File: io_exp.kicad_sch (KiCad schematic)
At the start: 14 parts, among them J26 Conn_01x03, J27 Conn_01x03, J28 Conn_01x03, J4 Conn_01x03, U11 PCF8574ATS

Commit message: [WiP] add expander
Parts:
- R40, R41, R42, R43, R44, R45, R46, R47: footprint (none) -> Resistor_SMD:R_0603_1608Metric

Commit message: Add BOM
Add LCSC reference and correct few footprint acording bom
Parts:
- C34: LCSC# (none) -> ?
- J26, J27, J28, J4: LCSC# (none) -> C144394
- U11: LCSC# (none) -> C2803277
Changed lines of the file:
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@@
+			)
+		)
+		(property "LCSC#" ""
+			(at 127 63.5 0)
+			(effects
+				(font
+					(size 1.27 1.27)
+				)
+				(hide yes)
 			)
 		)
@@
 		)
 		(property "Description" "Resistor, small symbol"
+			(at 128.27 105.41 0)
+			(effects
+				(font
+					(size 1.27 1.27)
+				)
+				(hide yes)
+			)
+		)
+		(property "LCSC#" ""
 			(at 128.27 105.41 0)
 			(effects
@@
 			)
 		)
+		(property "LCSC#" "C144394"
+			(at 142.24 80.01 0)
+			(effects
+				(font
+					(size 1.27 1.27)
+				)
+				(hide yes)
+			)
+		)
 		(pin "3"
 		)
@@
 		)
 		(property "Description" "Resistor, small symbol"
+			(at 133.35 63.5 0)
+			(effects
+				(font
+					(size 1.27 1.27)
+				)
+				(hide yes)
+			)
+		)
+		(property "LCSC#" ""
 			(at 133.35 63.5 0)
 			(effects
@@
 			)
 		)
+		(property "LCSC#" "?"
+			(at 74.93 55.88 0)
+			(effects
+				(font
+					(size 1.27 1.27)
+				)
+				(hide yes)
+			)
+		)
 		(pin "1"
 		)
@@
 			)
 		)
+		(property "LCSC#" ""
+			(at 134.62 91.44 0)
+			(effects
+				(font
+					(size 1.27 1.27)
+				)
+				(hide yes)
+			)
+		)
 		(pin "2"
 		)
@@
 		)
 		(property "Description" "Resistor, small symbol"
+			(at 134.62 105.41 0)
+			(effects
+				(font
+					(size 1.27 1.27)
+				)
+				(hide yes)
+			)
+		)
+		(property "LCSC#" ""
 			(at 134.62 105.41 0)
 			(effects
@@
 			)
 		)
+		(property "LCSC#" "C144394"
+			(at 142.24 66.04 0)
+			(effects
+				(font
+					(size 1.27 1.27)
+				)
+				(hide yes)
+			)
+		)
 		(pin "3"
 		)
@@
 			)
 		)
+		(property "LCSC#" "C2803277"
+			(at 92.71 78.74 0)
+			(effects
+				(font
+					(size 1.27 1.27)
+				)
+				(hide yes)
+			)
+		)
 		(pin "1"
 		)
@@
 			)
 		)
+		(property "LCSC#" ""
+			(at 128.27 91.44 0)
+			(effects
+				(font
+					(size 1.27 1.27)
+				)
+				(hide yes)
+			)
+		)
 		(pin "2"
 		)
@@
 			)
 		)
+		(property "LCSC#" ""
+			(at 133.35 77.47 0)
+			(effects
+				(font
+					(size 1.27 1.27)
+				)
+				(hide yes)
+			)
+		)
 		(pin "2"
 		)
@@
 		)
 		(property "Description" "Resistor, small symbol"
+			(at 127 77.47 0)
+			(effects
+				(font
+					(size 1.27 1.27)
+				)
+				(hide yes)
+			)
+		)
+		(property "LCSC#" ""
 			(at 127 77.47 0)
 			(effects
@@
 			)
 		)
+		(property "LCSC#" "C144394"
+			(at 143.51 93.98 0)
+			(effects
+				(font
+					(size 1.27 1.27)
+				)
+				(hide yes)
+			)
+		)
 		(pin "3"
 		)
@@
 			(at 143.51 107.95 0)
 			(effects
+				(font
+					(size 1.27 1.27)
+				)
+				(hide yes)
+			)
+		)
+		(property "LCSC#" "C144394"
+			(at 143.51 107.95 0)
+			(effects

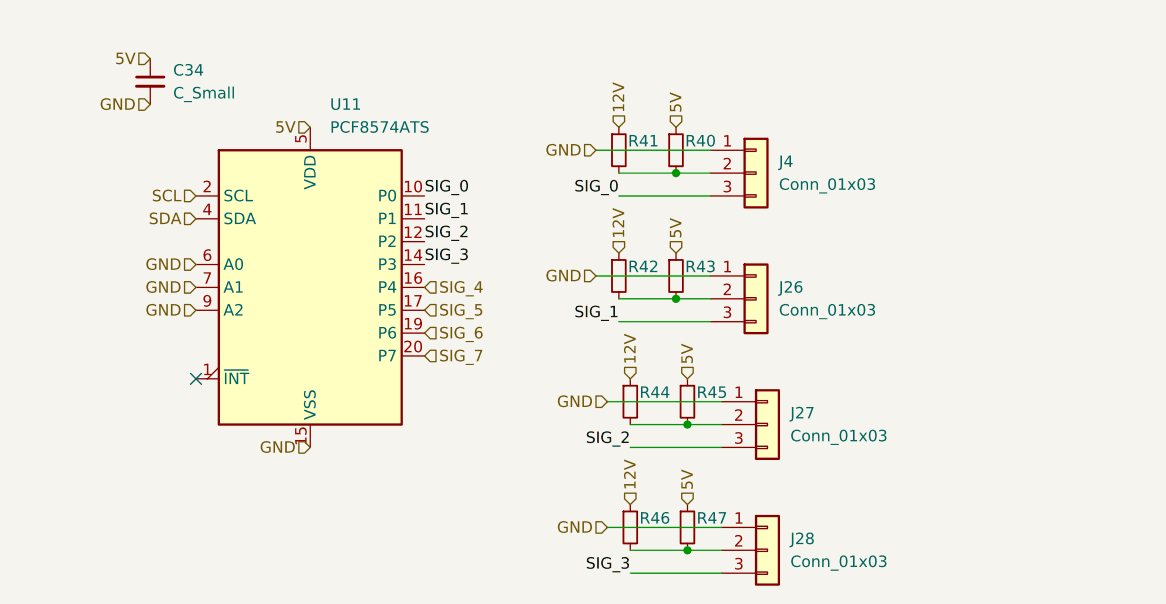
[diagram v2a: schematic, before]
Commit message: Go to 3.3V + fix io_exp + routing
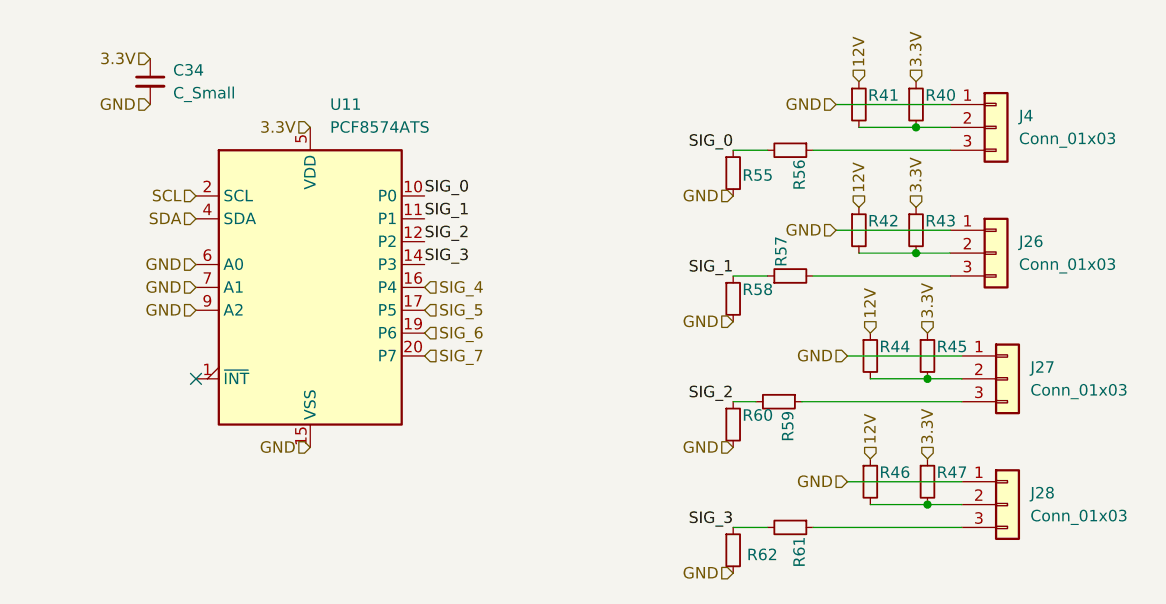
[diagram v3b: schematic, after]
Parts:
- added R55, R58, R60, R62: 22k, Resistor_SMD:R_0603_1608Metric, symbol Device:R_Small
- added R56, R57, R59, R61: 56.2k, Resistor_SMD:R_0603_1608Metric, symbol Device:R_Small
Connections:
- net GND: now also R55.2, R58.2, R60.2, R62.2
- net SIG_0: now also R55.1, R56.2; no longer J4.3 (Pin_3)
- net SIG_1: now also R57.1, R58.1; no longer J26.3 (Pin_3)
- net SIG_2: now also R59.2, R60.1; no longer J27.3 (Pin_3)
- net SIG_3: now also R61.2, R62.1; no longer J28.3 (Pin_3)
- net 5V renamed 3.3V
- new net: J26.3 (Pin_3), R57.2
- new net: J4.3 (Pin_3), R56.1
- new net: J27.3 (Pin_3), R59.1
- new net: J28.3 (Pin_3), R61.1
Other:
- moved on the sheet: J26, J27, J28, J4, R40, R41, R42, R43, R44, R45, R46, R47

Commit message: add values
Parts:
- R40, R43, R45, R47: value R_Small -> 3.3V
- R41, R42, R44, R46: value R_Small -> 12V
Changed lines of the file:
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@@
 			)
 		)
-		(property "Value" "R_Small"
+		(property "Value" "12V"
 			(at 156.21 59.6899 0)
 			(effects
@@
 			)
 		)
-		(property "Value" "R_Small"
+		(property "Value" "12V"
 			(at 157.48 101.5999 0)
 			(effects
@@
 			)
 		)
-		(property "Value" "R_Small"
+		(property "Value" "3.3V"
 			(at 162.56 59.6899 0)
 			(effects
@@
 			)
 		)
-		(property "Value" "R_Small"
+		(property "Value" "3.3V"
 			(at 163.83 87.6299 0)
 			(effects
@@
 			)
 		)
-		(property "Value" "R_Small"
+		(property "Value" "3.3V"
 			(at 163.83 101.5999 0)
 			(effects
@@
 			)
 		)
-		(property "Value" "R_Small"
+		(property "Value" "12V"
 			(at 157.48 87.6299 0)
 			(effects
@@
 			)
 		)
-		(property "Value" "R_Small"
+		(property "Value" "3.3V"
 			(at 162.56 73.6599 0)
 			(effects
@@
 			)
 		)
-		(property "Value" "R_Small"
+		(property "Value" "12V"
 			(at 156.21 73.6599 0)
 			(effects

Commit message: add missing pullup on IO_exp INT
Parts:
- added R50: 10k, Resistor_SMD:R_0603_1608Metric, symbol Device:R_Small
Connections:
- net 3.3V: now also R50.1
- net at U11.1 (~{INT}): now also R50.2
- no-connect marks 1 -> 0
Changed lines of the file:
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@@
 		(color 0 0 0 0)
 	)
-	(no_connect
-		(at 80.01 88.9)
+	(wire
+		(pts
+			(xy 76.2 88.9) (xy 80.01 88.9)
+		)
+		(stroke
+			(width 0)
+			(type default)
+		)
+	)
+	(wire
+		(pts
+			(xy 71.12 88.9) (xy 67.31 88.9)
+		)
+		(stroke
+			(width 0)
+			(type default)
+		)
 	)
 	(wire
@@
 		(shape input)
 		(at 92.71 60.96 180)
+		(effects
+			(font
+				(size 1.27 1.27)
+			)
+			(justify right)
+		)
+	)
+	(hierarchical_label "3.3V"
+		(shape input)
+		(at 67.31 88.9 180)
 		(effects
 			(font
@@
 					(unit 1)
 				)
+			)
+		)
+	)
+	(symbol
+		(lib_id "Device:R_Small")
+		(at 73.66 88.9 90)
+		(unit 1)
+		(exclude_from_sim no)
+		(in_bom yes)
+		(on_board yes)
+		(dnp no)
+		(property "Reference" "R50"
+			(at 72.644 87.884 0)
+			(effects
+				(font
+					(size 1.27 1.27)
+				)
+				(justify left)
+			)
+		)
+		(property "Value" "10k"
+			(at 74.9299 86.36 0)
+			(effects
+				(font
+					(size 1.27 1.27)
+				)
+				(justify left)
+				(hide yes)
+			)
+		)
+		(property "Footprint" "Resistor_SMD:R_0603_1608Metric"
+			(at 73.66 88.9 0)
+			(effects
+				(font
+					(size 1.27 1.27)
+				)
+				(hide yes)
+			)
+		)
+		(property "Datasheet" "~"
+			(at 73.66 88.9 0)
+			(effects
+				(font
+					(size 1.27 1.27)
+				)
+				(hide yes)
+			)
+		)
+		(property "Description" "Resistor, small symbol"
+			(at 73.66 88.9 0)
+			(effects
+				(font
+					(size 1.27 1.27)
+				)
+				(hide yes)
+			)
+		)
+		(property "LCSC#" ""
+			(at 73.66 88.9 0)
+			(effects
+				(font
+					(size 1.27 1.27)
+				)
+				(hide yes)
+			)
+		)
+		(pin "2"
+		)
+		(pin "1"
+		)
+		(instances
+			(project "carte_servo"
+				(path "/e63e39d7-6ac0-4ffd-8aa3-1841a4541b55/b45a520f-1905-47db-bbc3-05cad8f90896"
+					(reference "R50")
+					(unit 1)
+				)

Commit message: update BOM
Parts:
- C34: value C_Small -> 2.2uF; LCSC# ? -> C19110
- R50: value 10k -> 10kR; LCSC# (none) -> C2930027
- R55, R58, R60, R62: value 22k -> 22kR; LCSC# (none) -> C2907128
- R56, R57, R59, R61: value 56.2k -> 56.2kR; LCSC# (none) -> C2930117
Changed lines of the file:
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@@
 			)
 		)
-		(property "Value" "22k"
+		(property "Value" "22kR"
 			(at 142.24 67.3099 0)
 			(effects
@@
 			)
 		)
-		(property "LCSC#" ""
+		(property "LCSC#" "C2907128"
 			(at 139.7 66.04 0)
 			(effects
@@
 			)
 		)
-		(property "Value" "C_Small"
+		(property "Value" "2.2uF"
 			(at 77.47 57.1562 0)
 			(effects
@@
 			)
 		)
-		(property "Description" "Unpolarized capacitor, small symbol"
+		(property "Description" "Overkill, but I kept the 0805 footprint"
 			(at 74.93 55.88 0)
 			(effects
@@
 			)
 		)
-		(property "LCSC#" "?"
+		(property "LCSC#" "C19110"
 			(at 74.93 55.88 0)
 			(effects
@@
 			)
 		)
-		(property "Value" "56.2k"
+		(property "Value" "56.2kR"
 			(at 144.7801 66.04 0)
 			(effects
@@
 			)
 		)
-		(property "LCSC#" ""
+		(property "LCSC#" "C2930117"
 			(at 146.05 63.5 0)
 			(effects
@@
 			)
 		)
-		(property "Value" "56.2k"
+		(property "Value" "56.2kR"
 			(at 143.5101 93.98 0)
 			(effects
@@
 			)
 		)
-		(property "LCSC#" ""
+		(property "LCSC#" "C2930117"
 			(at 144.78 91.44 0)
 			(effects
@@
 			)
 		)
-		(property "Value" "10k"
+		(property "Value" "10kR"
 			(at 74.9299 86.36 0)
 			(effects
@@
 			)
 		)
-		(property "LCSC#" ""
+		(property "LCSC#" "C2930027"
 			(at 73.66 88.9 0)
 			(effects
@@
 			)
 		)
-		(property "Value" "56.2k"
+		(property "Value" "56.2kR"
 			(at 147.3199 74.93 0)
 			(effects
@@
 			)
 		)
-		(property "LCSC#" ""
+		(property "LCSC#" "C2930117"
 			(at 146.05 77.47 0)
 			(effects
@@
 			)
 		)
-		(property "Value" "22k"
+		(property "Value" "22kR"
 			(at 142.24 95.2499 0)
 			(effects
@@
 			)
 		)
-		(property "LCSC#" ""
+		(property "LCSC#" "C2907128"
 			(at 139.7 93.98 0)
 			(effects
@@
 			)
 		)
-		(property "Value" "22k"
+		(property "Value" "22kR"
 			(at 142.24 81.2799 0)
 			(effects
@@
 			)
 		)
-		(property "LCSC#" ""
+		(property "LCSC#" "C2907128"
 			(at 139.7 80.01 0)
 			(effects
@@
 			)
 		)
-		(property "Value" "22k"
+		(property "Value" "22kR"
 			(at 142.24 109.2199 0)
 			(effects
@@
 			)
 		)
-		(property "LCSC#" ""
+		(property "LCSC#" "C2907128"
 			(at 139.7 107.95 0)
 			(effects
@@
 			)
 		)
-		(property "Value" "56.2k"
+		(property "Value" "56.2kR"
 			(at 144.7801 107.95 0)
 			(effects
@@
 			)
 		)
-		(property "LCSC#" ""
+		(property "LCSC#" "C2930117"
 			(at 146.05 105.41 0)
 			(effects

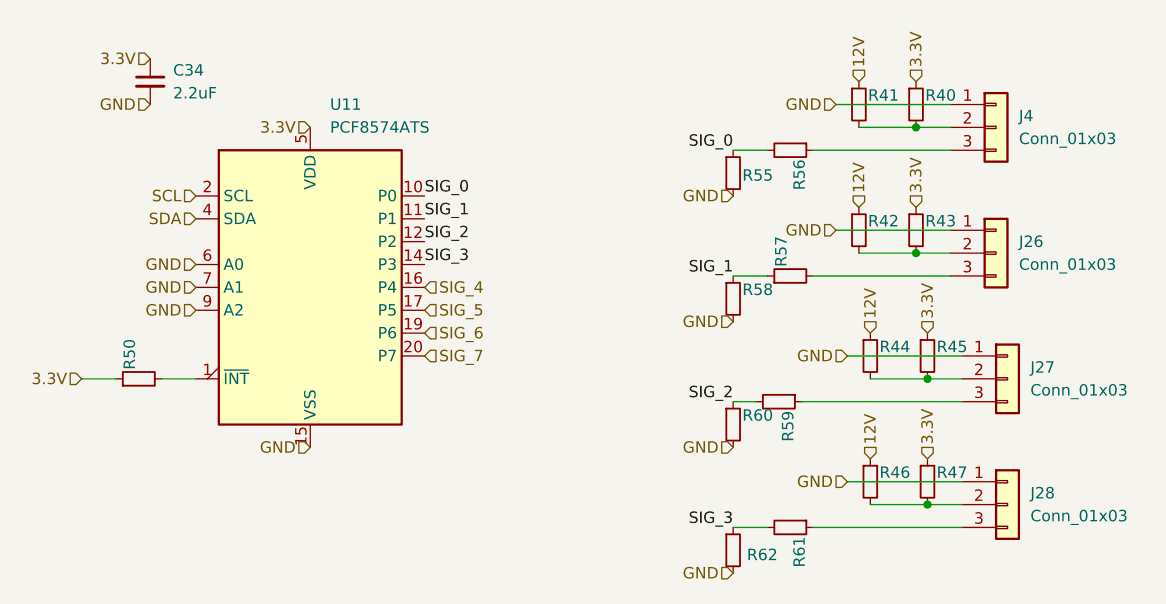
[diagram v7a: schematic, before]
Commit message: update BOM + add big capas (do not take DNP into account)
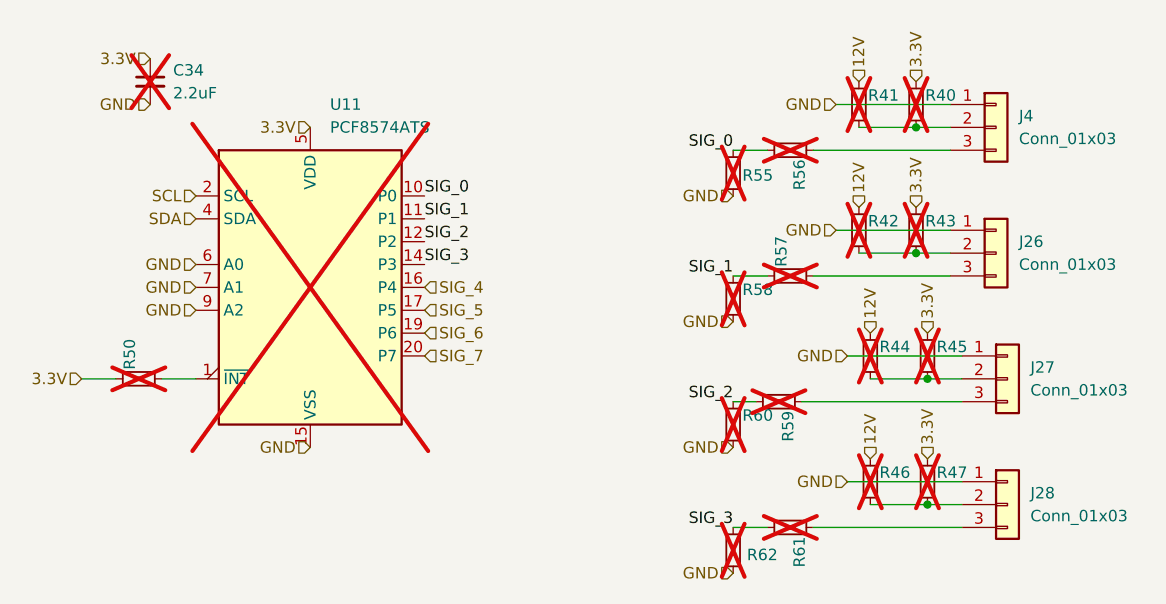
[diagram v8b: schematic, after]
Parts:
- C34, R40, R41, R42, R43, R44, R45, R46, R47, R50, R55, R56, R57, R58, R59, R60, R61, R62, U11: now not fitted
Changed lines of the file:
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@@
 		(in_bom yes)
 		(on_board yes)
-		(dnp no)
+		(dnp yes)
 		(property "Reference" "R41"
 			(at 154.686 57.404 0)
@@
 		(in_bom yes)
 		(on_board yes)
-		(dnp no)
+		(dnp yes)
 		(property "Reference" "R46"
 			(at 155.956 99.314 0)
@@
 		(in_bom yes)
 		(on_board yes)
-		(dnp no)
+		(dnp yes)
 		(property "Reference" "R40"
 			(at 161.036 57.404 0)
@@
 		(in_bom yes)
 		(on_board yes)
-		(dnp no)
+		(dnp yes)
 		(property "Reference" "R55"
 			(at 140.716 66.294 0)
@@
 		(in_bom yes)
 		(on_board yes)
-		(dnp no)
+		(dnp yes)
 		(fields_autoplaced yes)
 		(property "Reference" "C34"
@@
 		(in_bom yes)
 		(on_board yes)
-		(dnp no)
+		(dnp yes)
 		(property "Reference" "R56"
 			(at 147.066 64.516 0)
@@
 		(in_bom yes)
 		(on_board yes)
-		(dnp no)
+		(dnp yes)
 		(property "Reference" "R45"
 			(at 162.306 85.344 0)
@@
 		(in_bom yes)
 		(on_board yes)
-		(dnp no)
+		(dnp yes)
 		(property "Reference" "R47"
 			(at 162.306 99.314 0)
@@
 		(in_bom yes)
 		(on_board yes)
-		(dnp no)
+		(dnp yes)
 		(property "Reference" "R59"
 			(at 145.796 92.456 0)
@@
 		(in_bom yes)
 		(on_board yes)
-		(dnp no)
+		(dnp yes)
 		(property "Reference" "R50"
 			(at 72.644 87.884 0)
@@
 		(in_bom yes)
 		(on_board yes)
-		(dnp no)
+		(dnp yes)
 		(fields_autoplaced yes)
 		(property "Reference" "U11"
@@
 		(in_bom yes)
 		(on_board yes)
-		(dnp no)
+		(dnp yes)
 		(property "Reference" "R57"
 			(at 145.034 76.454 0)
@@
 		(in_bom yes)
 		(on_board yes)
-		(dnp no)
+		(dnp yes)
 		(property "Reference" "R60"
 			(at 140.716 92.964 0)
@@
 		(in_bom yes)
 		(on_board yes)
-		(dnp no)
+		(dnp yes)
 		(property "Reference" "R58"
 			(at 140.716 78.994 0)
@@
 		(in_bom yes)
 		(on_board yes)
-		(dnp no)
+		(dnp yes)
 		(property "Reference" "R44"
 			(at 155.956 85.344 0)
@@
 		(in_bom yes)
 		(on_board yes)
-		(dnp no)
+		(dnp yes)
 		(property "Reference" "R43"
 			(at 161.036 71.374 0)
@@
 		(in_bom yes)
 		(on_board yes)
-		(dnp no)
+		(dnp yes)
 		(property "Reference" "R42"
 			(at 154.686 71.374 0)
@@
 		(in_bom yes)
 		(on_board yes)
-		(dnp no)
+		(dnp yes)
 		(property "Reference" "R62"
 			(at 141.224 108.458 0)
@@
 		(in_bom yes)
 		(on_board yes)
-		(dnp no)
+		(dnp yes)
 		(property "Reference" "R61"
 			(at 147.066 106.426 0)
